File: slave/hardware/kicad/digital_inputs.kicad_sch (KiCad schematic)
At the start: 0 parts

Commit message: feat(HW): add protected high-speed and low-speed digital input circuits
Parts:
- added C34, C35, C36, C37: 100pF, Capacitor_SMD:C_0201_0603Metric, symbol Device:C
- added D37, D38, D43, D44: BAT54S, Package_TO_SOT_SMD:SOT-23, symbol Diode:BAT54S
- added IC6: ESDALC6V1W5_SPLIT, SOT65P210X110-5N, symbol Datalogger:ESDALC6V1W5_SPLIT
- added R72, R73, R75, R76, R78, R79, R89, R90: 1kR, Resistor_SMD:R_1210_3225Metric, symbol Device:R
- added R74, R77, R88, R91: 100kR, Resistor_SMD:R_0805_2012Metric, symbol Device:R
- added TP10, TP11, TP12, TP13, TP14, TP15, TP16, TP17: (no value), TestPoint:TestPoint_Pad_2.0x2.0mm, symbol Connector:TestPoint_Probe
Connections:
- new net: IC6.3, R75.1, R76.2
- new net: IC6.4, R78.1, R79.2
- new net: IC6.5, R89.1, R90.2
- new net: IC6.1, R72.1, R73.2
- new net +3.3V: D37.2 (K), D38.2 (K), D43.2 (K), D44.2 (K)
- new net FIELD_INPUT_01: R72.2, TP10.1
- new net FIELD_INPUT_02: R75.2, TP12.1
- new net FIELD_INPUT_03: R78.2, TP14.1
- new net FIELD_INPUT_04: R89.2, TP16.1
- new net GNDREF: C34.2, C35.2, C36.2, C37.2, D37.1 (A), D38.1 (A), D43.1 (A), D44.1 (A), IC6.2, IC6.2, IC6.2, IC6.2, R74.2, R77.2, R88.2, R91.2
- new net MCU_HS_01: C34.1, D37.3 (COM), R73.1, R74.1, TP11.1
- new net MCU_HS_02: C35.1, D38.3 (COM), R76.1, R77.1, TP13.1
- new net MCU_HS_03: C36.1, D43.3 (COM), R79.1, R88.1, TP15.1
- new net MCU_HS_04: C37.1, D44.3 (COM), R90.1, R91.1, TP17.1
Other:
- note added: "Fc = 1 / 2πRC"
- note added: "HIGH_SPEED_INPUT"
- note added: "R1 = (Vs - Vtvs) / I"
- note added: "R2 = Vr / I"

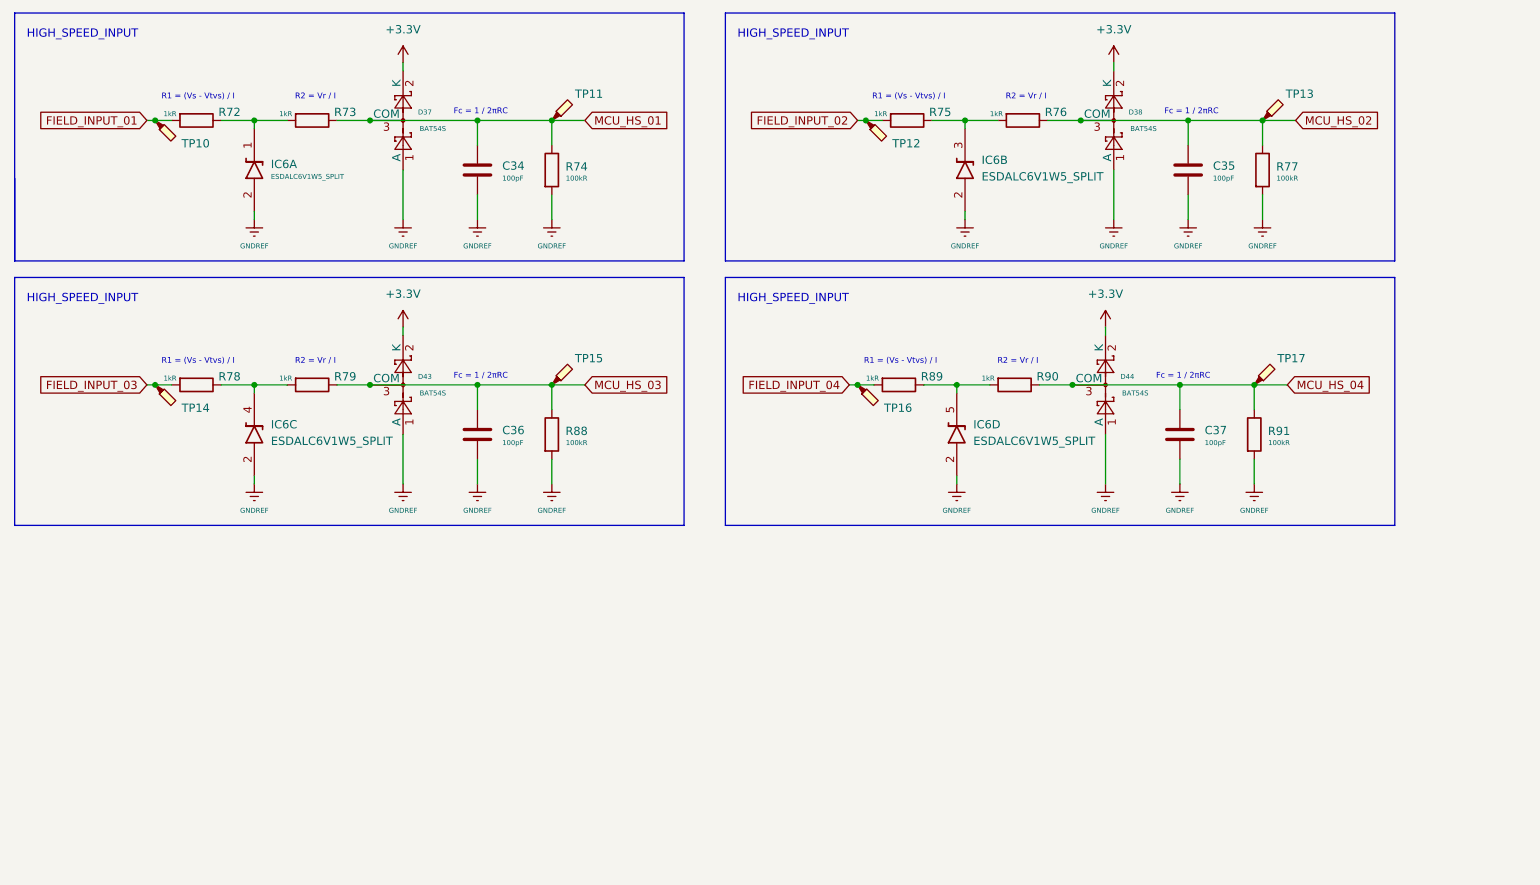
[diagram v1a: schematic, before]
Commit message: refactor(HW): position adjustment
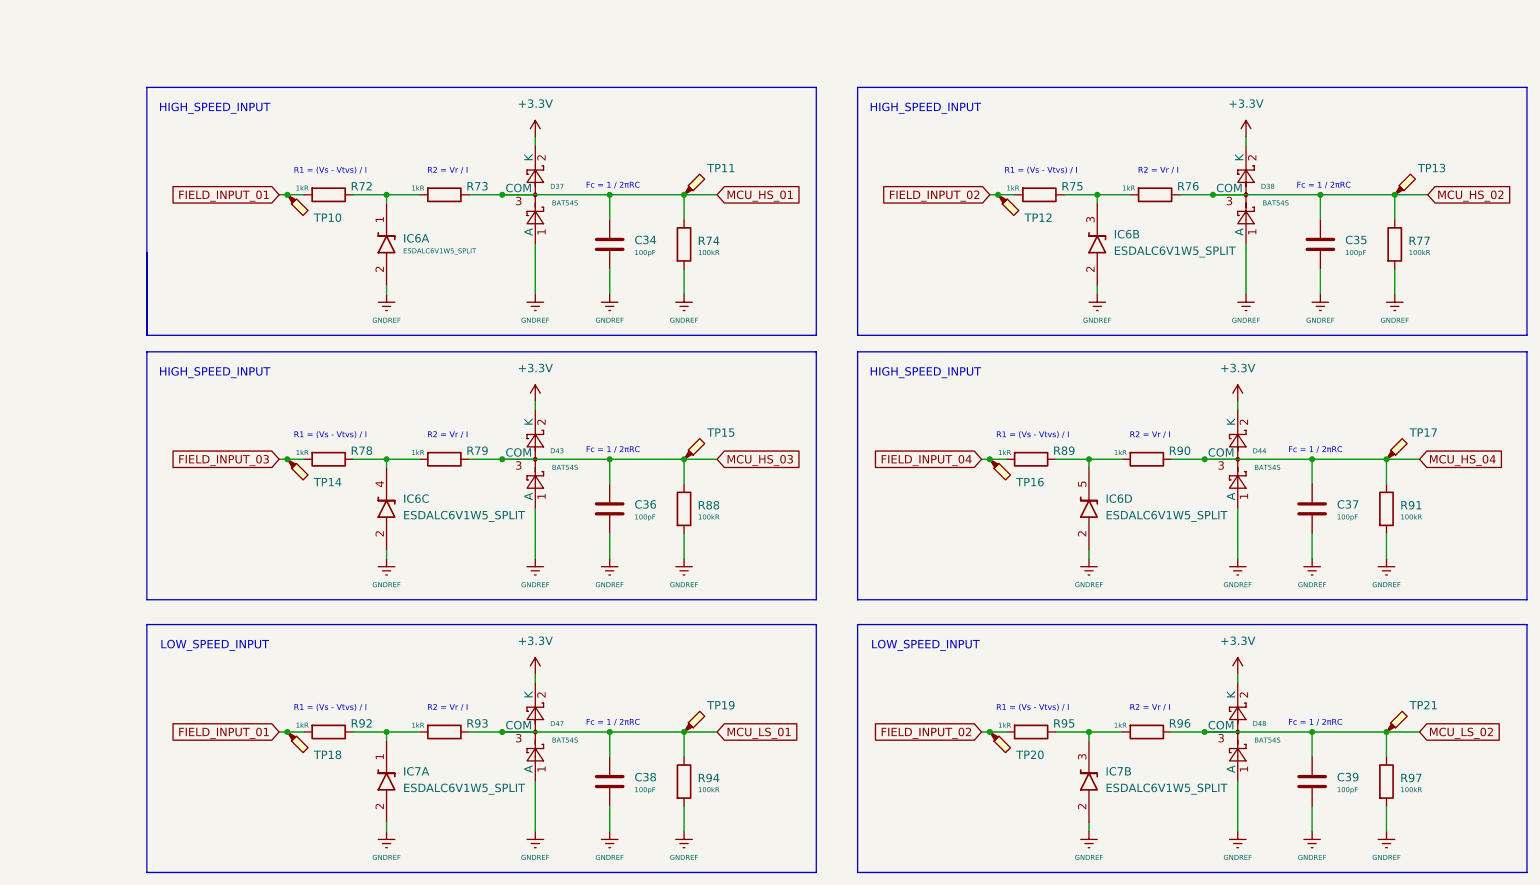
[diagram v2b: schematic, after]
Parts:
- added C38, C39: 100pF, Capacitor_SMD:C_0201_0603Metric, symbol Device:C
- added D47, D48: BAT54S, Package_TO_SOT_SMD:SOT-23, symbol Diode:BAT54S
- added IC7: ESDALC6V1W5_SPLIT, SOT65P210X110-5N, symbol Datalogger:ESDALC6V1W5_SPLIT
- added R92, R93, R95, R96: 1kR, Resistor_SMD:R_1210_3225Metric, symbol Device:R
- added R94, R97: 100kR, Resistor_SMD:R_0805_2012Metric, symbol Device:R
- added TP18, TP19, TP20, TP21: (no value), TestPoint:TestPoint_Pad_2.0x2.0mm, symbol Connector:TestPoint_Probe
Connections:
- net +3.3V: now also D47.2 (K), D48.2 (K)
- net FIELD_INPUT_01: now also R92.2, TP18.1
- net FIELD_INPUT_02: now also R95.2, TP20.1
- net GNDREF: now also C38.2, C39.2, D47.1 (A), D48.1 (A), IC7.2, IC7.2, R94.2, R97.2
- new net: IC7.3, R95.1, R96.2
- new net: IC7.1, R92.1, R93.2
- new net MCU_LS_01: C38.1, D47.3 (COM), R93.1, R94.1, TP19.1
- new net MCU_LS_02: C39.1, D48.3 (COM), R96.1, R97.1, TP21.1
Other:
- note added: "LOW_SPEED_INPUT"
- moved on the sheet: C34, C35, C36, C37, D37, D38, D43, D44, IC6A, IC6B, IC6C, IC6D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

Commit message: refactor(HW): rename components and fix reference designators
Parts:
- renumbered C34 to C50, C36 to C51, C38 to C52, C37 to C53, C39 to C54, C35 to C55, D37 to D23, D43 to D24, D47 to D25, D44 to D26, D48 to D27, D38 to D28, IC6 to IC10, IC7 to IC11, R72 to R42, R78 to R43, R92 to R44, R73 to R45, R79 to R46, R93 to R47, R74 to R48, R88 to R49, R94 to R50, R89 to R51, R95 to R52, R75 to R53, R90 to R54, R96 to R55, R76 to R56, R91 to R57, R97 to R58, R77 to R59, TP10 to TP26, TP14 to TP27, TP18 to TP28, TP11 to TP29, TP15 to TP30, TP19 to TP31, TP16 to TP32, TP20 to TP33, TP12 to TP34, TP17 to TP35, TP21 to TP36, TP13 to TP37
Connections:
- net FIELD_INPUT_01: no longer R44.2, TP28.1
- net FIELD_INPUT_02: no longer R52.2, TP33.1
- new net FIELD_INPUT_05: R44.2, TP28.1
- new net FIELD_INPUT_06: R52.2, TP33.1

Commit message: feat(HW): add footprints and configure component properties
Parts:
- IC10, IC11: footprint SOT65P210X110-5N -> Datalogger:SOT65P210X110-5N
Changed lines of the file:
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@@
 			)
 		)
-		(property "Footprint" "SOT65P210X110-5N"
+		(property "Footprint" "Datalogger:SOT65P210X110-5N"
 			(at 81.28 118.11 0)
 			(hide yes)
@@
 			)
 		)
-		(property "Footprint" "SOT65P210X110-5N"
+		(property "Footprint" "Datalogger:SOT65P210X110-5N"
 			(at 189.23 118.11 0)
 			(hide yes)
@@
 			)
 		)
-		(property "Footprint" "SOT65P210X110-5N"
+		(property "Footprint" "Datalogger:SOT65P210X110-5N"
 			(at 189.23 160.02 0)
 			(hide yes)
@@
 			)
 		)
-		(property "Footprint" "SOT65P210X110-5N"
+		(property "Footprint" "Datalogger:SOT65P210X110-5N"
 			(at 81.28 77.47 0)
 			(hide yes)
@@
 			)
 		)
-		(property "Footprint" "SOT65P210X110-5N"
+		(property "Footprint" "Datalogger:SOT65P210X110-5N"
 			(at 190.5 77.47 0)
 			(hide yes)
@@
 			)
 		)
-		(property "Footprint" "SOT65P210X110-5N"
+		(property "Footprint" "Datalogger:SOT65P210X110-5N"
 			(at 81.28 160.02 0)
 			(hide yes)

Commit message: feat(HW): finalize schematic design
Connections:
- net MCU_HS_03 is gone; now on net MCU_LS_01: C51.1, D24.3 (COM), R46.1, R49.1, TP30.1
- net MCU_HS_04 is gone; now on net MCU_HS_02: C53.1, D26.3 (COM), R54.1, R57.1, TP35.1
- net MCU_LS_01: no longer C52.1, D25.3 (COM), R47.1, R50.1, TP31.1
- net MCU_LS_02 renamed MCU_LS_04
- new net MCU_LS_03: C52.1, D25.3 (COM), R47.1, R50.1, TP31.1
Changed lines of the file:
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@@
 		)
 	)
-	(global_label "MCU_LS_02"
+	(global_label "MCU_LS_04"
 		(shape input)
 		(at 236.22 134.62 0)
@@
 		)
 	)
-	(global_label "MCU_LS_01"
+	(global_label "MCU_LS_03"
 		(shape input)
 		(at 128.27 134.62 0)
@@
 		)
 	)
-	(global_label "MCU_HS_03"
+	(global_label "MCU_LS_01"
 		(shape input)
 		(at 128.27 92.71 0)
@@
 		)
 		(property "Intersheetrefs" "${INTERSHEET_REFS}"
-			(at 142.2013 92.71 0)
+			(at 141.8989 92.71 0)
 			(hide yes)
 			(show_name no)
@@
 		)
 	)
-	(global_label "MCU_HS_04"
+	(global_label "MCU_HS_02"
 		(shape input)
 		(at 236.22 92.71 0)

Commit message: fix(HW): resolve KiCad ERC warnings
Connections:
- net MCU_HS_02: no longer C53.1, D26.3 (COM), R54.1, R57.1, TP35.1
- new net MCU_LS_02: C53.1, D26.3 (COM), R54.1, R57.1, TP35.1
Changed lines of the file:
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@@
 		)
 	)
-	(global_label "MCU_HS_02"
+	(global_label "MCU_LS_02"
 		(shape input)
 		(at 236.22 92.71 0)
@@
 		)
 		(property "Intersheetrefs" "${INTERSHEET_REFS}"
-			(at 250.1513 92.71 0)
+			(at 249.8489 92.71 0)
 			(hide yes)
 			(show_name no)

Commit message: feat(HW): begin PCB layout design
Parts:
- C50, C51, C52, C53, C54, C55: footprint Capacitor_SMD:C_0201_0603Metric -> Capacitor_SMD:C_0603_1608Metric
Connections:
- net at R53.1, R56.2: now also IC10.5; no longer IC10.3
- net at R52.1, R55.2: now also IC10.3; no longer IC11.3
- net at R51.1, R54.2: now also IC11.3; no longer IC10.5
